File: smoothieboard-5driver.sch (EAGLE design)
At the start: 285 parts, among them IC1 LPC1769, IC10 LM1117-3.3V, IC11 78L12F, IC12 A4982, IC13 R-78E-5.0, IC2 A4982, IC3 A4982, IC4 MCP44X1, IC5 A4982, IC6 A4982, IC9 MCP44X1, J10 POWER_JACKSMD, Q1 BSL207SP, Q10 SUD50P04-08-GE3, Q2 12MHz, Q3 25MHz, Q4 ZXMN4A06, Q5 AOT240L, Q6 AOT240L, Q7 AOT240L, Q8 ZXMN4A06, Q9 ZXMN4A06, U1 USD-SOCKETNEW, X14 USBPTH

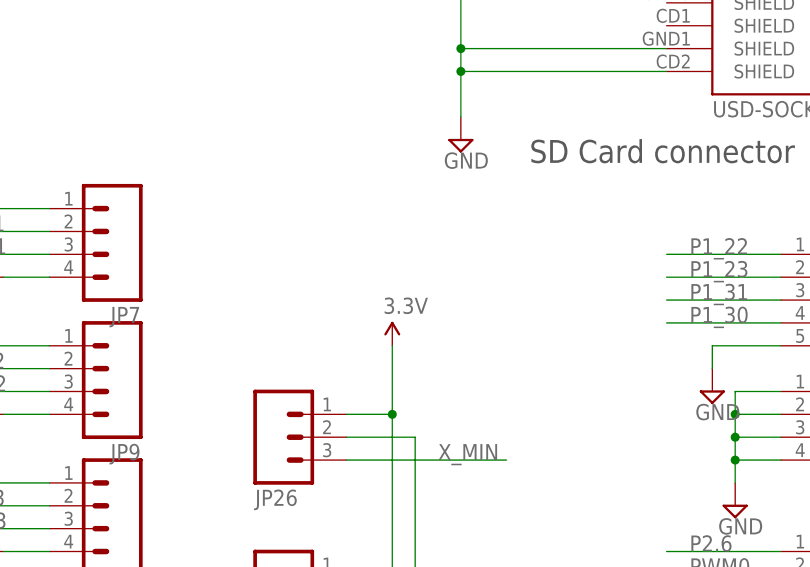
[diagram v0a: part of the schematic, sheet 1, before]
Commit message: Add solder jumper for endstop voltage selection, move labels to _tsilk layer instead of tnames
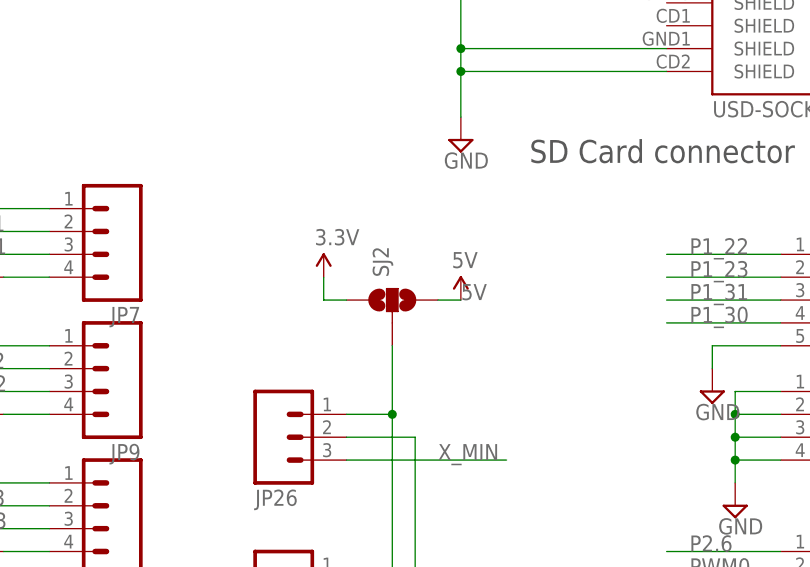
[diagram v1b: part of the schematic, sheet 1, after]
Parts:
- added SJ2: (no value), SparkFun:SOLDERJUMPER_2WAYS
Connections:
- new net N$115: JP14.1, JP16.1, JP19.1, JP21.1, JP22.1, JP26.1, SJ2.2
- net 3.3V: now also SJ2.1; no longer JP14.1, JP16.1, JP19.1, JP21.1, JP22.1, JP26.1
- net 5V: now also SJ2.3

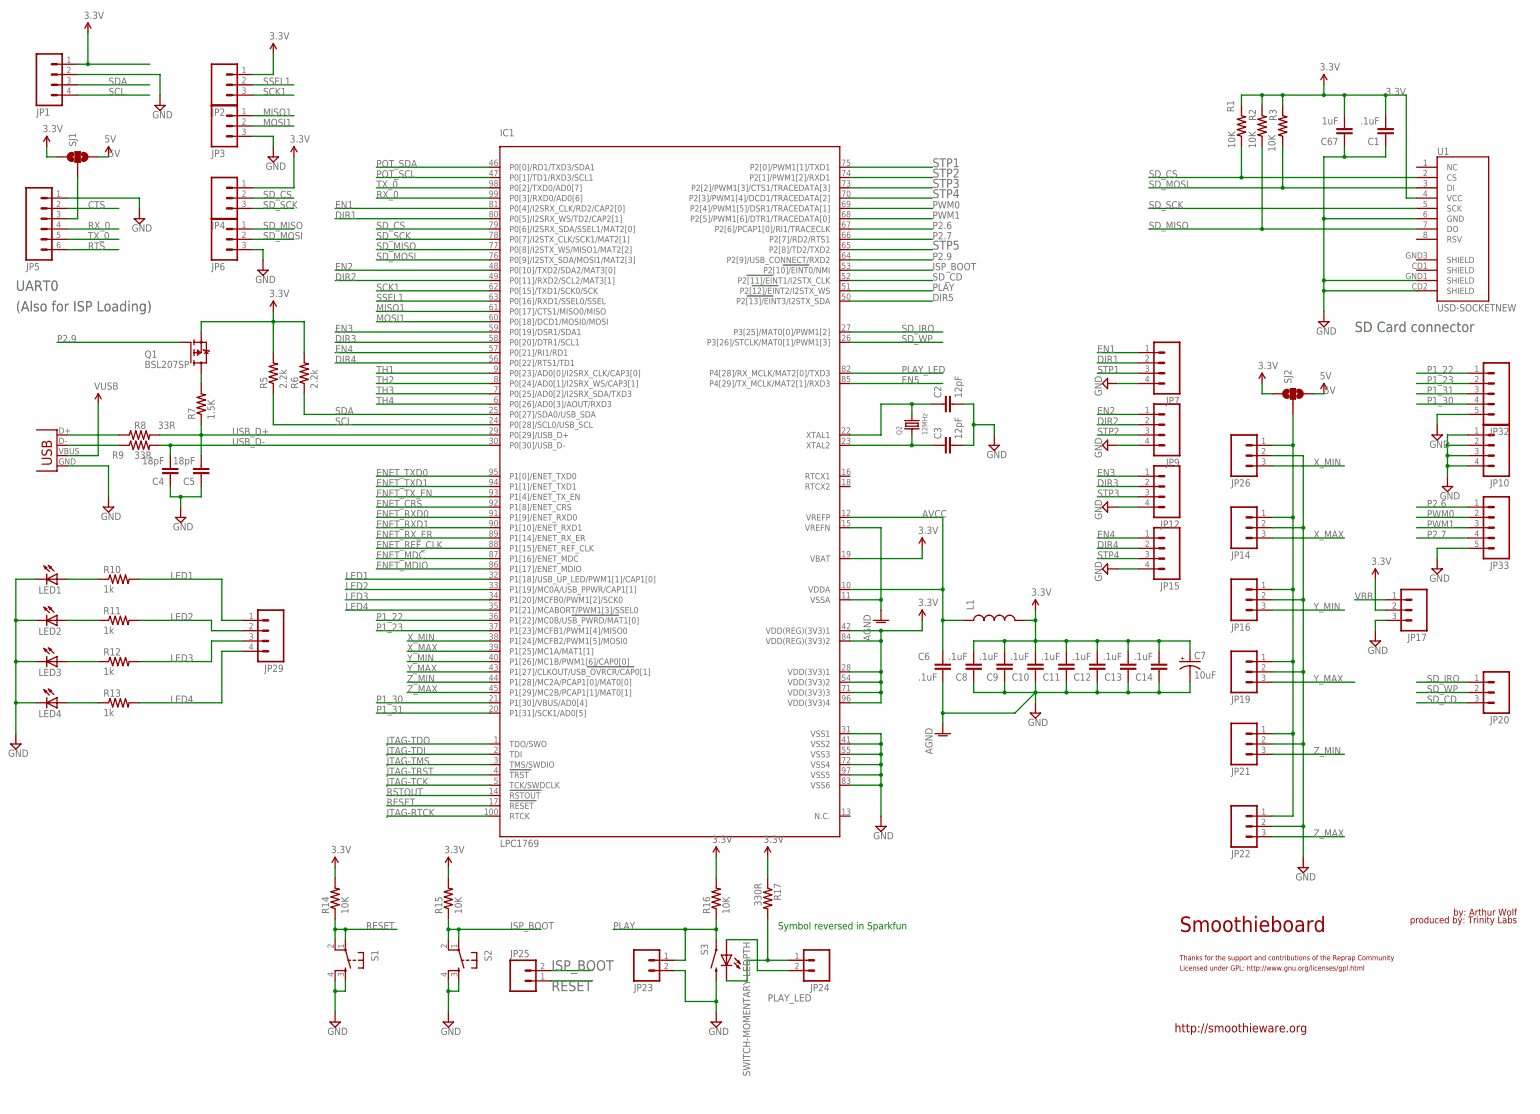
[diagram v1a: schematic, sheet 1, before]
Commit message: Add input protection to endstops
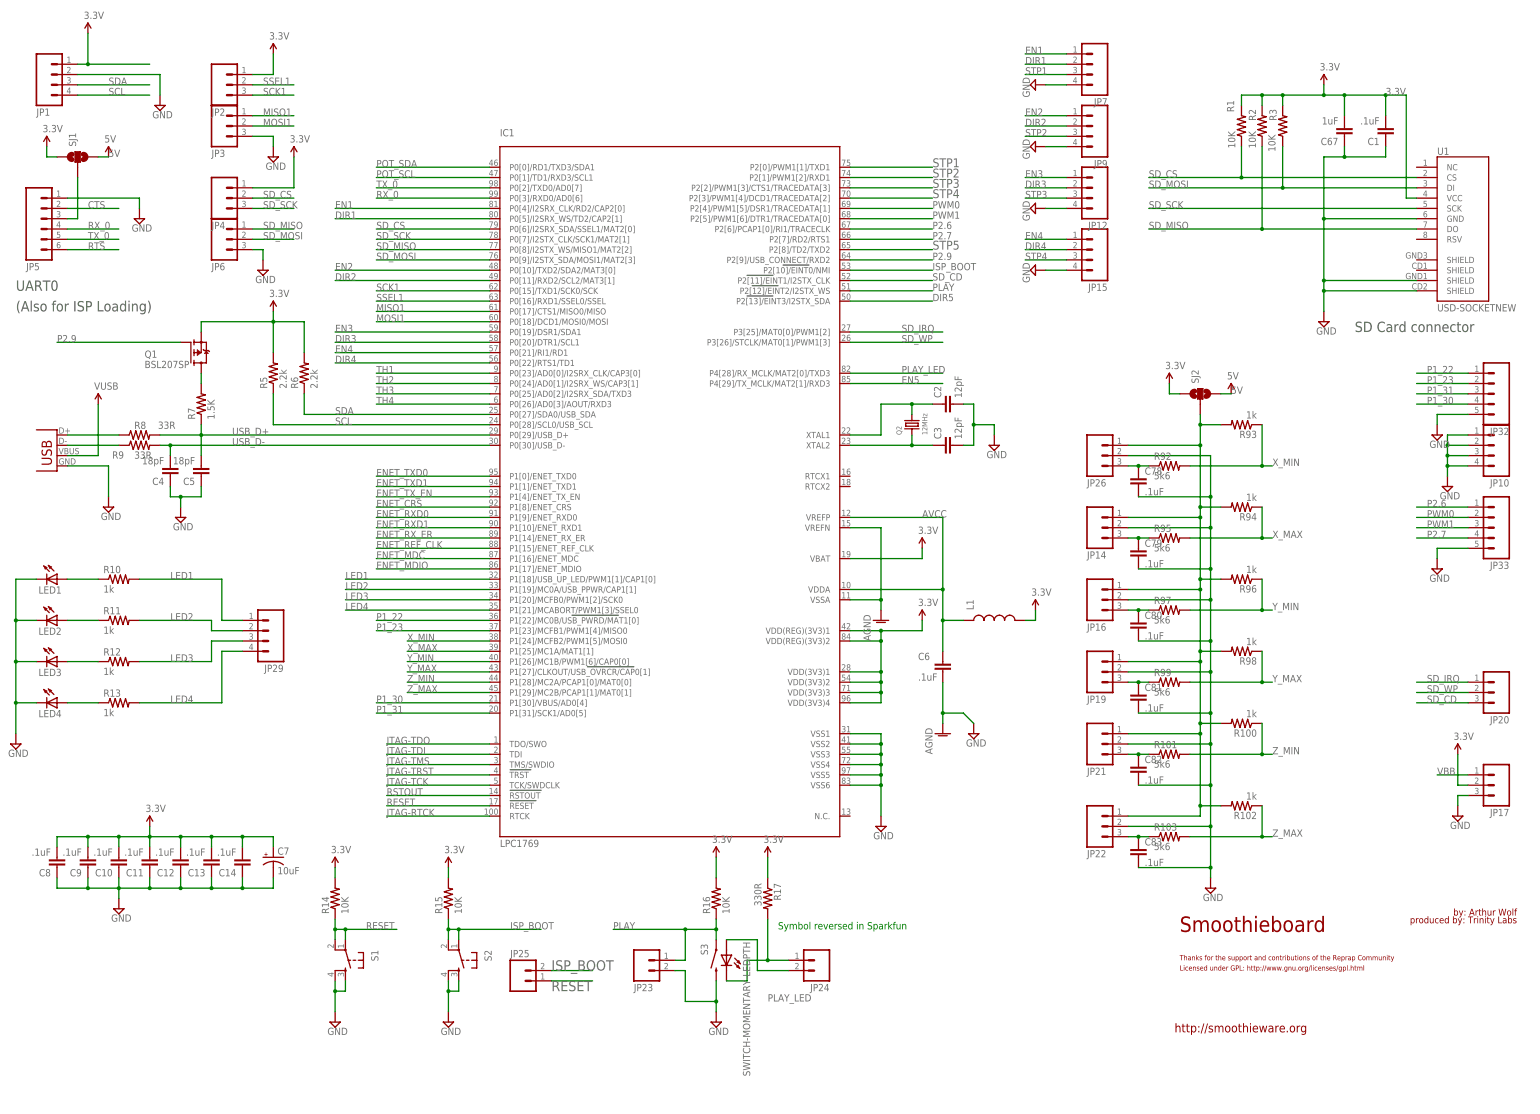
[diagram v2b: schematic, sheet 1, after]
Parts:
- added C78, C79, C80, C81, C82, C83: .1uF, rcl:C-EUC0603
- added R100, R102, R93, R94, R96, R98: 1k, resistor:R-US_R0603
- added R101, R103, R92, R95, R97, R99: 5k6, resistor:R-US_R0603
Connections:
- new net N$114: C79.1, JP14.3, R95.1
- new net N$116: C80.1, JP16.3, R97.1
- new net N$117: C81.1, JP19.3, R99.1
- new net N$118: C83.1, JP22.3, R103.1
- new net N$119: C82.1, JP21.3, R101.1
- new net N$122: C78.1, JP26.3, R92.1
- net GND: now also C78.2, C79.2, C80.2, C81.2, C82.2, C83.2
- net N$115: now also R100.2, R102.2, R93.2, R94.2, R96.2, R98.2
- net X_MAX: now also R94.1, R95.2; no longer JP14.3
- net X_MIN: now also R92.2, R93.1; no longer JP26.3
- net Y_MAX: now also R98.1, R99.2; no longer JP19.3
- net Y_MIN: now also R96.1, R97.2; no longer JP16.3
- net Z_MAX: now also R102.1, R103.2; no longer JP22.3
- net Z_MIN: now also R100.1, R101.2; no longer JP21.3
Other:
- moved on the sheet: C10, C11, C12, C13, C14, C7, C8, C9, JP12, JP14, JP15, JP16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

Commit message: Move a couple of names off pads, short solder jumpers for x16 microstep by default, ensure A4982's thermal pads have tStop
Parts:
- renumbered U$2 to IC14, U$8 to IC15
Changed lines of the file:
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@@
 <part name="JP30" library="SparkFun" deviceset="JUMPER-2" device="SMD-NC"/>
 <part name="JP31" library="SparkFun" deviceset="JUMPER-2" device="SMD-NC"/>
-<part name="U$2" library="custom_esorensen" deviceset="TC4427" device=""/>
+<part name="IC14" library="custom_esorensen" deviceset="TC4427" device=""/>
 <part name="AGND1" library="supply1" deviceset="AGND" device=""/>
 <part name="AGND2" library="supply1" deviceset="AGND" device=""/>
@@
 <part name="U$7" library="eric_sorensen" deviceset="5MMCONN" device=""/>
 <part name="R86" library="resistor" deviceset="R-US_" device="R0603" value="10k"/>
-<part name="U$8" library="custom_esorensen" deviceset="TC4427" device=""/>
+<part name="IC15" library="custom_esorensen" deviceset="TC4427" device=""/>
 <part name="C75" library="resistor" deviceset="C-EU" device="C0603" value=".1uF"/>
 <part name="SUPPLY83" library="supply2" deviceset="GND" device=""/>
@@
 <instance part="SUPPLY78" gate="GND" x="149.86" y="63.5"/>
 <instance part="C66" gate="G$1" x="190.5" y="119.38"/>
-<instance part="U$2" gate="RAILS" x="198.12" y="119.38"/>
-<instance part="U$2" gate="A" x="86.36" y="86.36"/>
-<instance part="U$2" gate="B" x="162.56" y="86.36"/>
+<instance part="IC14" gate="RAILS" x="198.12" y="119.38"/>
+<instance part="IC14" gate="A" x="86.36" y="86.36"/>
+<instance part="IC14" gate="B" x="162.56" y="86.36"/>
 <instance part="IC11" gate="G$1" x="170.18" y="142.24"/>
 <instance part="U$3" gate="G$1" x="43.18" y="38.1"/>
@@
 <wire x1="190.5" y1="104.14" x2="198.12" y2="104.14" width="0.1524" layer="91"/>
 <wire x1="198.12" y1="104.14" x2="198.12" y2="99.06" width="0.1524" layer="91"/>
-<pinref part="U$2" gate="RAILS" pin="P$2"/>
+<pinref part="IC14" gate="RAILS" pin="P$2"/>
 <wire x1="198.12" y1="104.14" x2="198.12" y2="106.68" width="0.1524" layer="91"/>
 <junction x="198.12" y="104.14"/>
@@
 <wire x1="149.86" y1="81.28" x2="149.86" y2="86.36" width="0.1524" layer="91"/>
 <wire x1="149.86" y1="86.36" x2="142.24" y2="86.36" width="0.1524" layer="91"/>
-<pinref part="U$2" gate="B" pin="P$1"/>
+<pinref part="IC14" gate="B" pin="P$1"/>
 <wire x1="152.4" y1="86.36" x2="149.86" y2="86.36" width="0.1524" layer="91"/>
 <junction x="149.86" y="86.36"/>
@@
 <wire x1="190.5" y1="134.62" x2="198.12" y2="134.62" width="0.1524" layer="91"/>
 <junction x="198.12" y="134.62"/>
-<pinref part="U$2" gate="RAILS" pin="P$1"/>
+<pinref part="IC14" gate="RAILS" pin="P$1"/>
 <pinref part="IC11" gate="G$1" pin="VO"/>
 <label x="187.96" y="142.24" size="1.27" layer="95"/>
@@
 <wire x1="73.66" y1="86.36" x2="63.5" y2="86.36" width="0.1524" layer="91"/>
 <label x="63.5" y="86.36" size="1.778" layer="95"/>
-<pinref part="U$2" gate="A" pin="P$1"/>
+<pinref part="IC14" gate="A" pin="P$1"/>
 <wire x1="76.2" y1="86.36" x2="73.66" y2="86.36" width="0.1524" layer="91"/>
 <junction x="73.66" y="86.36"/>
@@
 <segment>
 <pinref part="R69" gate="G$1" pin="1"/>
-<pinref part="U$2" gate="A" pin="P$2"/>
+<pinref part="IC14" gate="A" pin="P$2"/>
 <wire x1="104.14" y1="86.36" x2="101.6" y2="86.36" width="0.1524" layer="91"/>
 </segment>
@@
 <net name="N$19" class="0">
 <segment>
-<pinref part="U$2" gate="B" pin="P$2"/>
+<pinref part="IC14" gate="B" pin="P$2"/>
 <pinref part="R70" gate="G$1" pin="1"/>
 <wire x1="177.8" y1="86.36" x2="180.34" y2="86.36" width="0.1524" layer="91"/>
@@
 <instance part="U$7" gate="G$1" x="284.48" y="203.2" rot="MR180"/>
 <instance part="R86" gate="G$1" x="264.16" y="177.8"/>
-<instance part="U$8" gate="A" x="241.3" y="198.12"/>
-<instance part="U$8" gate="RAILS" x="170.18" y="187.96"/>
+<instance part="IC15" gate="A" x="241.3" y="198.12"/>
+<instance part="IC15" gate="RAILS" x="170.18" y="187.96"/>
 <instance part="C75" gate="G$1" x="162.56" y="187.96"/>
 <instance part="SUPPLY83" gate="GND" x="167.64" y="167.64"/>
@@
 </segment>
 <segment>
-<pinref part="U$8" gate="RAILS" pin="P$2"/>
+<pinref part="IC15" gate="RAILS" pin="P$2"/>
 <wire x1="170.18" y1="175.26" x2="170.18" y2="172.72" width="0.1524" layer="91"/>
 <pinref part="C75" gate="G$1" pin="2"/>
@@
 <net name="12VREG" class="0">
 <segment>
-<pinref part="U$8" gate="RAILS" pin="P$1"/>
+<pinref part="IC15" gate="RAILS" pin="P$1"/>
 <wire x1="170.18" y1="200.66" x2="170.18" y2="203.2" width="0.1524" layer="91"/>
 <pinref part="C75" gate="G$1" pin="1"/>
@@
 <net name="P1_23" class="0">
 <segment>
-<pinref part="U$8" gate="A" pin="P$1"/>
+<pinref part="IC15" gate="A" pin="P$1"/>
 <pinref part="R87" gate="G$1" pin="2"/>
 <wire x1="231.14" y1="198.12" x2="228.6" y2="198.12" width="0.1524" layer="91"/>
@@
 <net name="N$113" class="0">
 <segment>
-<pinref part="U$8" gate="A" pin="P$2"/>
+<pinref part="IC15" gate="A" pin="P$2"/>
 <pinref part="R88" gate="G$1" pin="2"/>
 <wire x1="256.54" y1="198.12" x2="259.08" y2="198.12" width="0.1524" layer="91"/>
